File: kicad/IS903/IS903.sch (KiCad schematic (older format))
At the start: 30 parts, among them J1 USB3_A, U1 IS903_QFN64_8*8, U2 EML3020, U3 EMP8733-1.2, U4 NAND_BGA152, U5 NAND_BGA152, Y1 30MHZ 2520

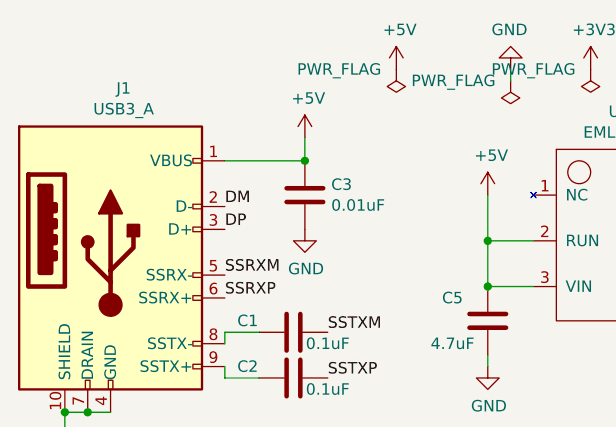
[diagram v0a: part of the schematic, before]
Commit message: 完成PCB布局
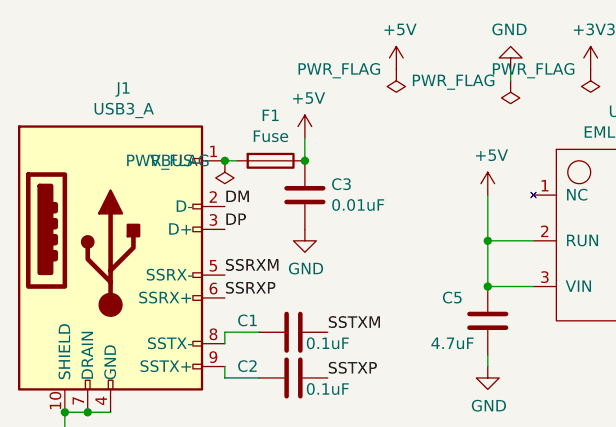
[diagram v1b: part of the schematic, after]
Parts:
- added F1: Fuse, Fuse:Fuse_0603_1608Metric, symbol Device:Fuse
- C5, C7: footprint Capacitor_SMD:C_0402_1005Metric -> Capacitor_SMD:C_0603_1608Metric
- D1: footprint Capacitor_SMD:C_0603_1608Metric -> LED_SMD:LED_0603_1608Metric
- J1: footprint Connector_USB:USB3_A_Plug_Wuerth_692112030100_Horizontal -> Connector_USB:USB3_A_Plug_Wuerth_692112030100_Horizontal_without_hole
- L1: footprint Capacitor_SMD:C_0603_1608Metric -> Inductor_SMD:L_1008_2520Metric
- U1: footprint (none) -> Package_DFN_QFN:QFN-64-1EP_8x8mm_P0.4mm_EP6.5x6.5mm
- U2: footprint Package_TO_SOT_SMD:SOT-23-5 -> Package_DFN_QFN:TDFN-6-1EP_2.5x2.5mm_P0.65mm_EP1.3x2mm
- U4, U5: footprint (none) -> Package_BGA:BGA-152_14x18mm_Layout13x17_P0.5mm
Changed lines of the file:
@@
 F 0 "J1" H 1357 2217 50  0000 C CNN
 F 1 "USB3_A" H 1357 2126 50  0000 C CNN
-F 2 "Connector_USB:USB3_A_Plug_Wuerth_692112030100_Horizontal" H 1450 1600 50  0001 C CNN
+F 2 "Connector_USB:USB3_A_Plug_Wuerth_692112030100_Horizontal_without_hole" H 1450 1600 50  0001 C CNN
 F 3 "~" H 1450 1600 50  0001 C CNN
 	1    1300 1500
@@
 F 0 "U2" H 3525 1915 50  0000 C CNN
 F 1 "EML3020" H 3525 1824 50  0000 C CNN
-F 2 "Package_TO_SOT_SMD:SOT-23-5" H 3650 1800 50  0001 C CNN
+F 2 "Package_DFN_QFN:TDFN-6-1EP_2.5x2.5mm_P0.65mm_EP1.3x2mm" H 3650 1800 50  0001 C CNN
 F 3 "" H 3650 1800 50  0001 C CNN
 	1    3550 1400
@@
 F 0 "L1" V 4450 1500 50  0000 C CNN
 F 1 "4.7uH" V 4300 1550 50  0000 C CNN
-F 2 "Capacitor_SMD:C_0603_1608Metric" H 4350 1550 50  0001 C CNN
+F 2 "Inductor_SMD:L_1008_2520Metric" H 4350 1550 50  0001 C CNN
 F 3 "~" H 4350 1550 50  0001 C CNN
 	1    4350 1550
@@
 F 0 "C5" H 2750 1900 50  0000 L CNN
 F 1 "4.7uF" H 2700 1700 50  0000 L CNN
-F 2 "Capacitor_SMD:C_0402_1005Metric" H 2988 1650 50  0001 C CNN
+F 2 "Capacitor_SMD:C_0603_1608Metric" H 2988 1650 50  0001 C CNN
 F 3 "~" H 2950 1800 50  0001 C CNN
 	1    2950 1800
@@
 F 0 "C7" H 3650 3250 50  0000 L CNN
 F 1 "4.7uF" H 3650 3050 50  0000 L CNN
-F 2 "Capacitor_SMD:C_0402_1005Metric" H 3888 3000 50  0001 C CNN
+F 2 "Capacitor_SMD:C_0603_1608Metric" H 3888 3000 50  0001 C CNN
 F 3 "~" H 3850 3150 50  0001 C CNN
 	1    3850 3150
@@
 F 0 "D1" H 8643 6067 50  0000 C CNN
 F 1 "LED_0603" H 8643 5976 50  0000 C CNN
-F 2 "Capacitor_SMD:C_0603_1608Metric" H 8650 5850 50  0001 C CNN
+F 2 "LED_SMD:LED_0603_1608Metric" H 8650 5850 50  0001 C CNN
 F 3 "~" H 8650 5850 50  0001 C CNN
 	1    8650 5850
@@
 Wire Wire Line
 	2150 1100 2150 1000
-Wire Wire Line
-	1800 1100 2150 1100
-Connection ~ 2150 1100
 $Comp
 L Device:C C11
@@
 F 0 "U1" H 2800 5350 50  0000 L CNN
 F 1 "IS903_QFN64_8*8" H 2700 5600 50  0000 L CNN
-F 2 "" H 4200 3800 50  0001 C CNN
+F 2 "Package_DFN_QFN:QFN-64-1EP_8x8mm_P0.4mm_EP6.5x6.5mm" H 4200 3800 50  0001 C CNN
 F 3 "" H 4200 3800 50  0001 C CNN
 	1    2750 5400
@@
 F 0 "U4" H 6725 4715 50  0000 C CNN
 F 1 "NAND_BGA152" H 6725 4624 50  0000 C CNN
-F 2 "" H 7150 350 50  0001 C CNN
+F 2 "Package_BGA:BGA-152_14x18mm_Layout13x17_P0.5mm" H 7150 350 50  0001 C CNN
 F 3 "" H 7150 350 50  0001 C CNN
 	1    6750 2650
@@
 F 0 "U5" H 9525 4765 50  0000 C CNN
 F 1 "NAND_BGA152" H 9525 4674 50  0000 C CNN
-F 2 "" H 9950 400 50  0001 C CNN
+F 2 "Package_BGA:BGA-152_14x18mm_Layout13x17_P0.5mm" H 9950 400 50  0001 C CNN
 F 3 "" H 9950 400 50  0001 C CNN
 	1    9550 2700
@@
 	1    0    0    -1
 $EndComp
+$Comp
+L Device:Fuse F1
+U 1 1 5F1B83BF
+P 2000 1100
+F 0 "F1" V 1803 1100 50  0000 C CNN
+F 1 "Fuse" V 1894 1100 50  0000 C CNN
+F 2 "Fuse:Fuse_0603_1608Metric" V 1930 1100 50  0001 C CNN
+F 3 "~" H 2000 1100 50  0001 C CNN
+	1    2000 1100
+	0    1    1    0
+$EndComp
+Connection ~ 2150 1100
+Wire Wire Line
+	1850 1100 1800 1100
+$Comp
+L power:PWR_FLAG #FLG0103
+U 1 1 5F1DE554
+P 1800 1100
+F 0 "#FLG0103" H 1800 1175 50  0001 C CNN
+F 1 "PWR_FLAG" H 2050 1100 50  0000 C CNN
+F 2 "" H 1800 1100 50  0001 C CNN
+F 3 "~" H 1800 1100 50  0001 C CNN
+	1    1800 1100
+	-1   0    0    1
+$EndComp
+Connection ~ 1800 1100
 $EndSCHEMATC
